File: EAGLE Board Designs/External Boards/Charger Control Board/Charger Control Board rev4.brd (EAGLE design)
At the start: 81 parts

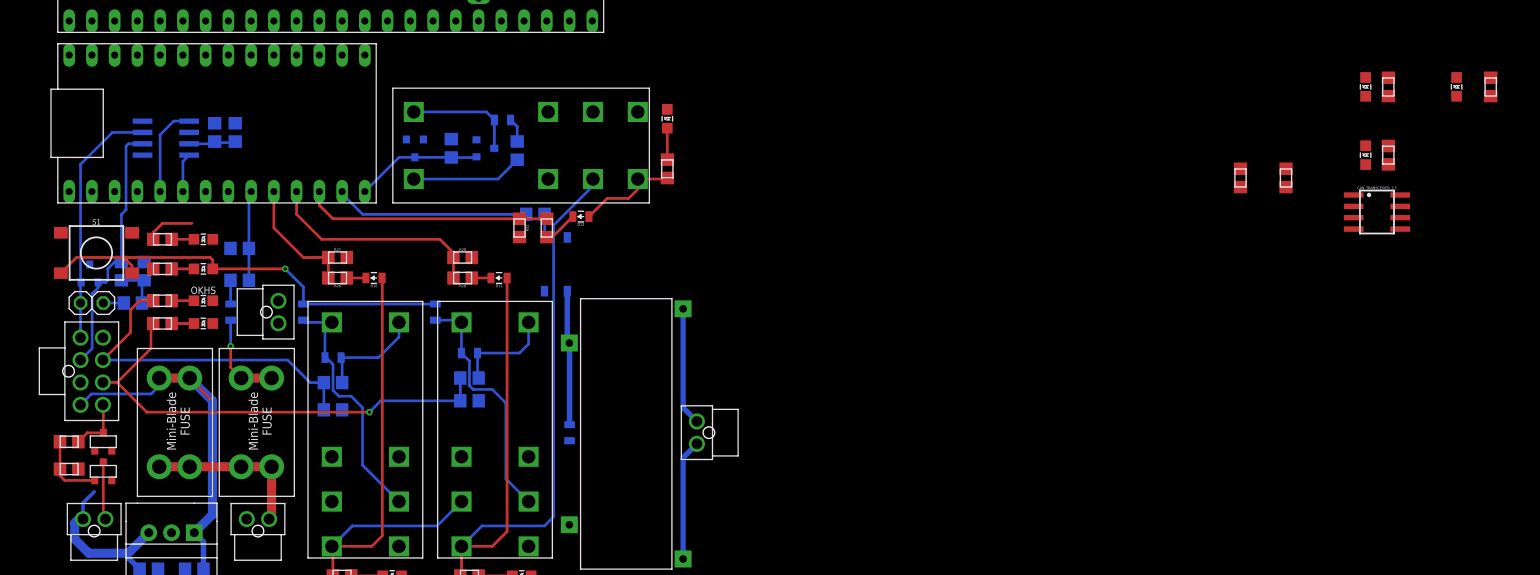
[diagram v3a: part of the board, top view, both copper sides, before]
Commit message: routed all LEDs
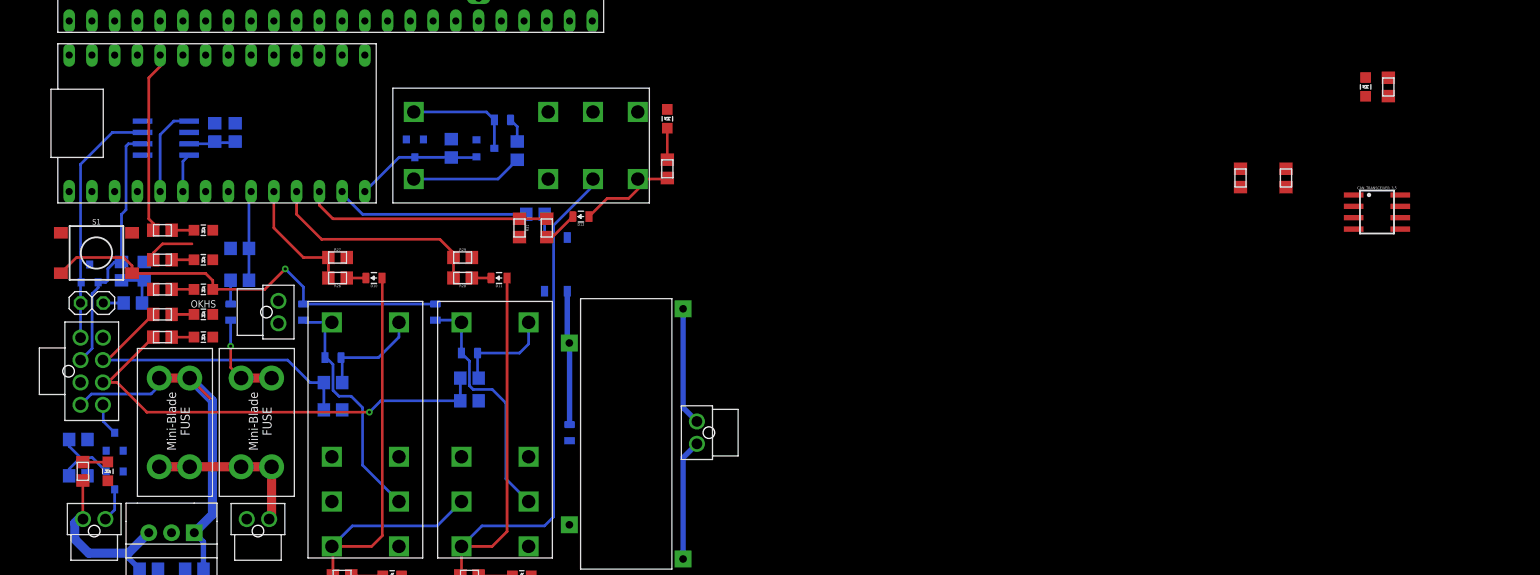
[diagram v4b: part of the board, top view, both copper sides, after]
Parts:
- moved R5 163.0 mm to (-74.7, 34.5), turned to 90 degrees
- moved POWER_5V 156.6 mm to (-71.9, 34.5), turned to 180 degrees
- moved R15 137.2 mm to (-65.8, 61.5), turned to 180 degrees
- moved STATUS_3.2 130.1 mm to (-61.2, 61.5), turned to 270 degrees
- moved LATCH 2.29 mm to (-61.2, 54.9)
- moved R34 2.29 mm to (-65.8, 58.2)
- moved R6 2.29 mm to (-65.8, 54.9)
- moved SOFTWARE 2.29 mm to (-61.2, 58.2)
- moved Q1 1.63 mm to (-71.1, 33.5), flipped to the bottom, turned to 180 degrees
- moved BMS_OK 1.52 mm to (-61.2, 49.5)
- moved OKHS 1.52 mm to (-61.2, 52.1)
- moved R7 1.52 mm to (-65.8, 52.1)
- moved R8 1.52 mm to (-65.8, 49.5)
- moved R12 1.27 mm to (-75.2, 34.0), flipped to the bottom, turned to 0 degrees
- moved ZENER 1.27 mm to (-71.1, 37.8), flipped to the bottom
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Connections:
- net N$11: now also U$4.A8; no longer U$4.A6
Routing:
- net N$11: track 0.00 -> 20.3 mm
- net N$29: track 0.00 -> 2.80 mm
- net N$1: track 6.43 -> 3.75 mm
- net CHARGE_ENABLE: track 6.34 -> 3.67 mm, vias 0 -> 1
- net N$8: track 0.00 -> 2.50 mm
- net OKHS: track 38.6 -> 36.8 mm
- net BMS_OK: track 52.9 -> 51.8 mm
- net +5V: track 23.9 -> 24.7 mm
- net N$5: track 7.91 -> 8.62 mm

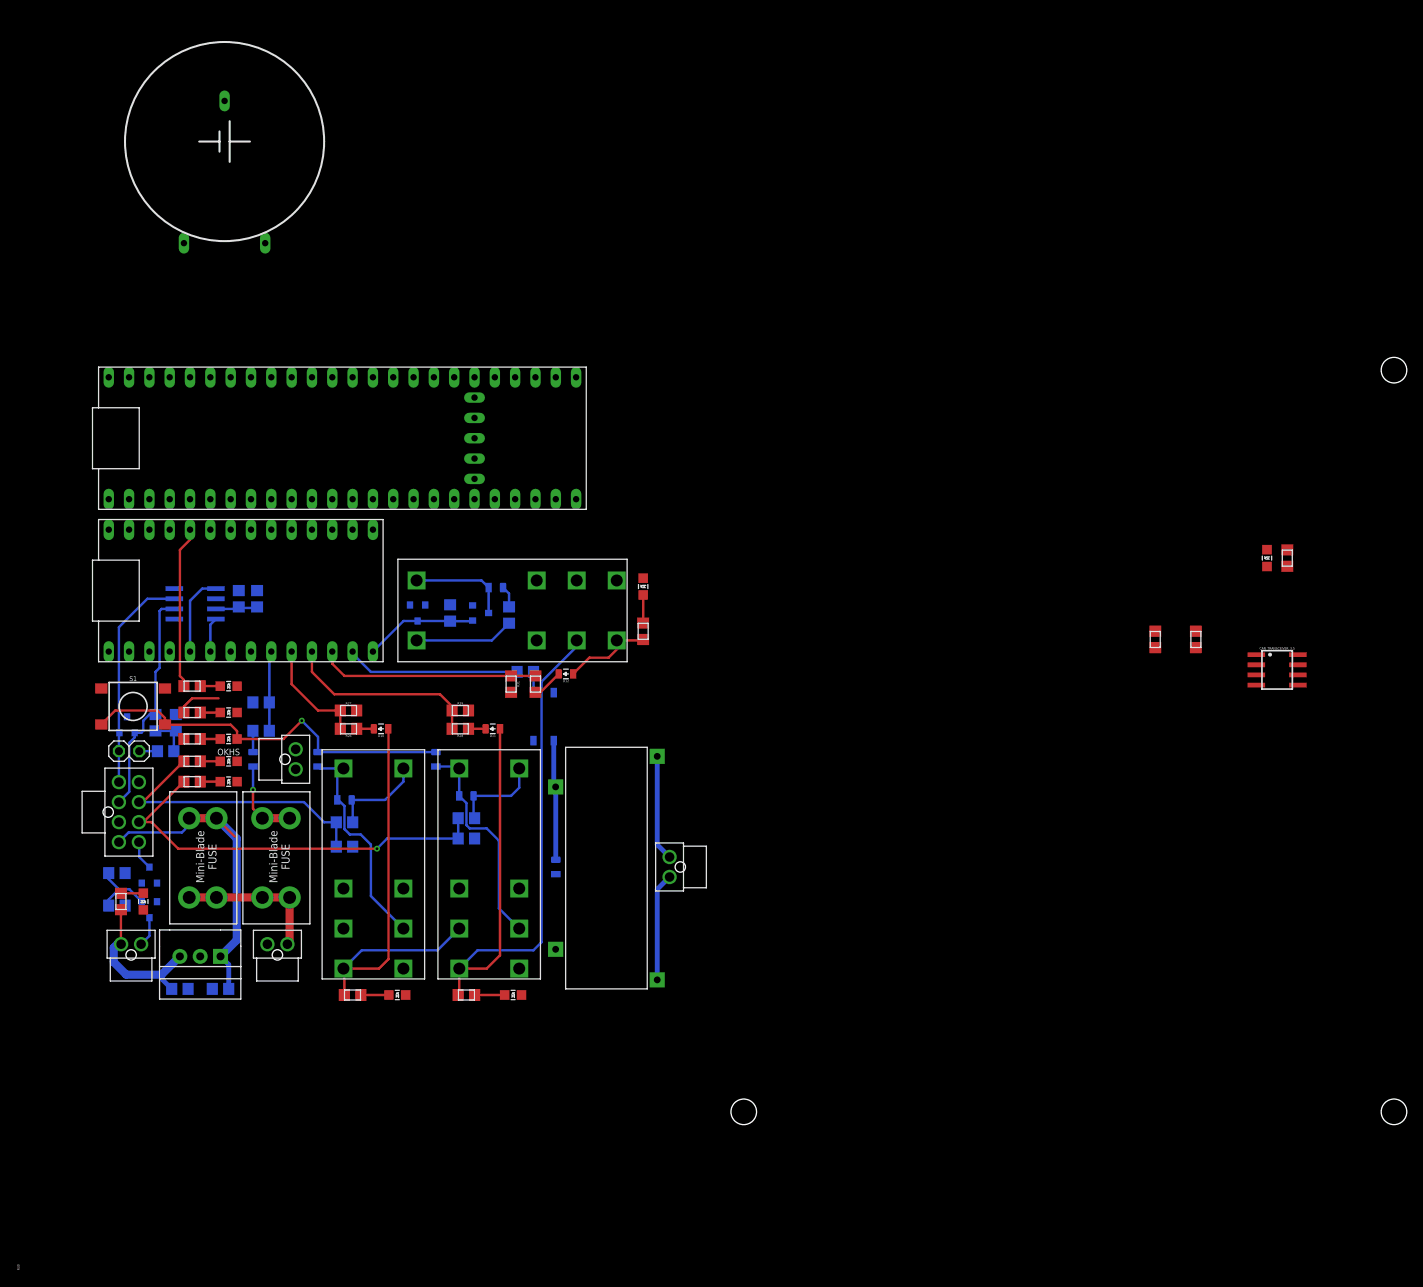
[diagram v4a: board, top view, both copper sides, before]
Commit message: Added ground plane
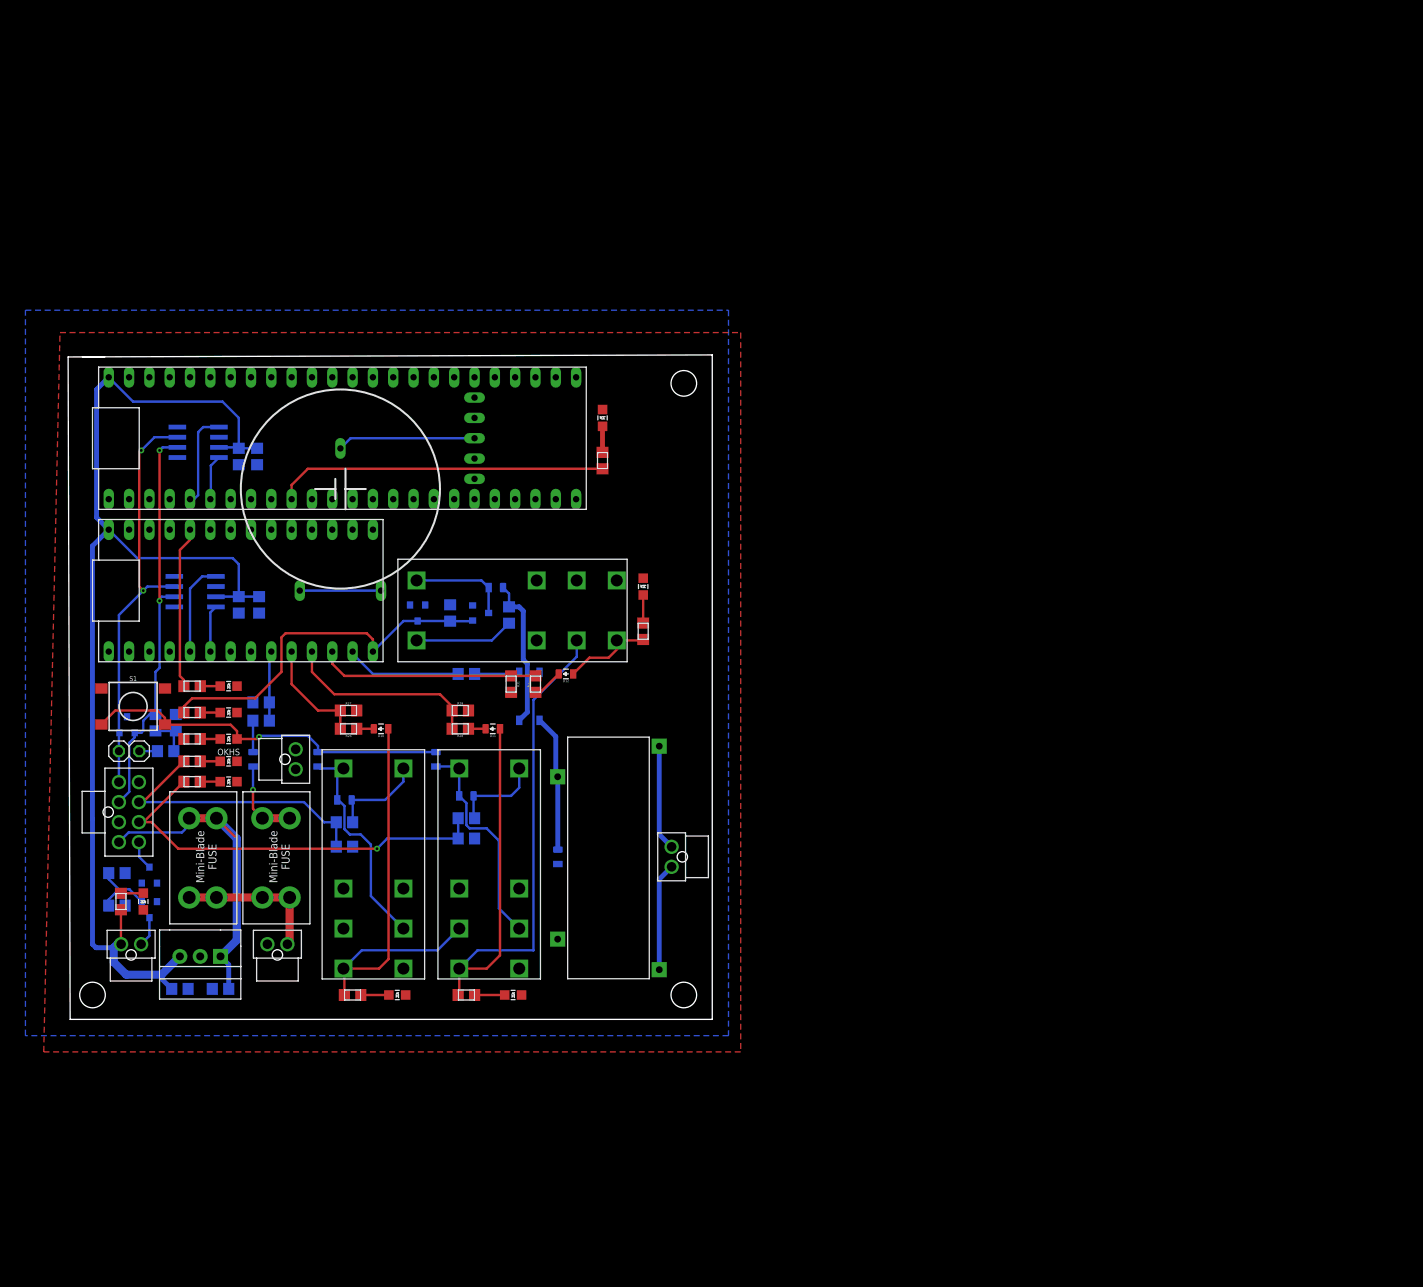
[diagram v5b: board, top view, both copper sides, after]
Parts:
- moved CAN_TRANSCEIVER_3.5 137.8 mm to (-65.0, 91.9), flipped to the bottom
- moved C6 121.8 mm to (-59.9, 90.2), flipped to the bottom, turned to 90 degrees
- moved C7 114.6 mm to (-57.7, 90.2), flipped to the bottom, turned to 90 degrees
- moved R17 86.5 mm to (-14.5, 89.7), turned to 270 degrees
- moved STATUS_3.5 84.9 mm to (-14.5, 95.0)
- moved U$16 45.8 mm to (-47.2, 86.1)
- moved R14 7.37 mm to (-31.5, 63.0)
- moved U$2 3.10 mm to (-23.6, 60.2)
- moved CAN_TRANSCEIVER_3.2 1.52 mm to (-65.4, 73.3)
- moved U$3 1.30 mm to (-8.64, 24.9)
- moved CHARGER 1.30 mm to (-5.84, 40.1)
- moved D3 1.30 mm to (-20.1, 40.1)
- moved R19 1.27 mm to (-57.1, 57.1)
- moved C1 0.80 mm to (-57.4, 71.6), turned to 90 degrees
- moved C2 0.76 mm to (-59.9, 71.6), turned to 90 degrees
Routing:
- net +5V: track 24.7 -> 149.5 mm
- net N$9: track 0.00 -> 41.5 mm
- net SOFTWARE_SHUTDOWN: track 19.6 -> 46.6 mm
- net CANH: track 27.9 -> 52.4 mm, vias 0 -> 2
- net CANL: track 28.9 -> 51.6 mm, vias 0 -> 2
- net N$61: track 0.00 -> 17.3 mm
- net +12V: track 43.5 -> 59.8 mm
- net N$6: track 0.00 -> 12.0 mm
- net VBAT_RTC: track 0.00 -> 10.2 mm
- net TOGGLE_CHARGER: track 21.8 -> 14.5 mm
- net N$4: track 0.00 -> 5.65 mm
- net N$7: track 0.00 -> 3.26 mm
- net N$10: track 2.59 -> 5.66 mm
- net LATCH_EXT_BUTTON: track 48.8 -> 46.5 mm
- net CHARGE_CONTROL: track 15.1 -> 17.2 mm
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- added copper zone on layer 1, net GND
- added copper zone on layer 16, net GND
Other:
- board outline added: 80.5 x 83.1 mm

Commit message: Pass DRC
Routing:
- net +12V: track 59.8 -> 107.2 mm, vias 0 -> 1
- net SHUTDOWN_D: track 11.3 -> 54.9 mm, vias 0 -> 2
- net SHUTDOWN_E: track 0.00 -> 25.1 mm
- net VBAT_RTC: track 10.2 -> 30.9 mm
- net SHUTDOWN_A: track 10.4 -> 27.9 mm
- net GND: track 0.00 -> 16.0 mm, vias 0 -> 1
- net +5V: track 149.5 -> 161.5 mm, vias 0 -> 1
- net CHARGE_ENABLE: track 3.67 -> 7.01 mm, vias 1 -> 0

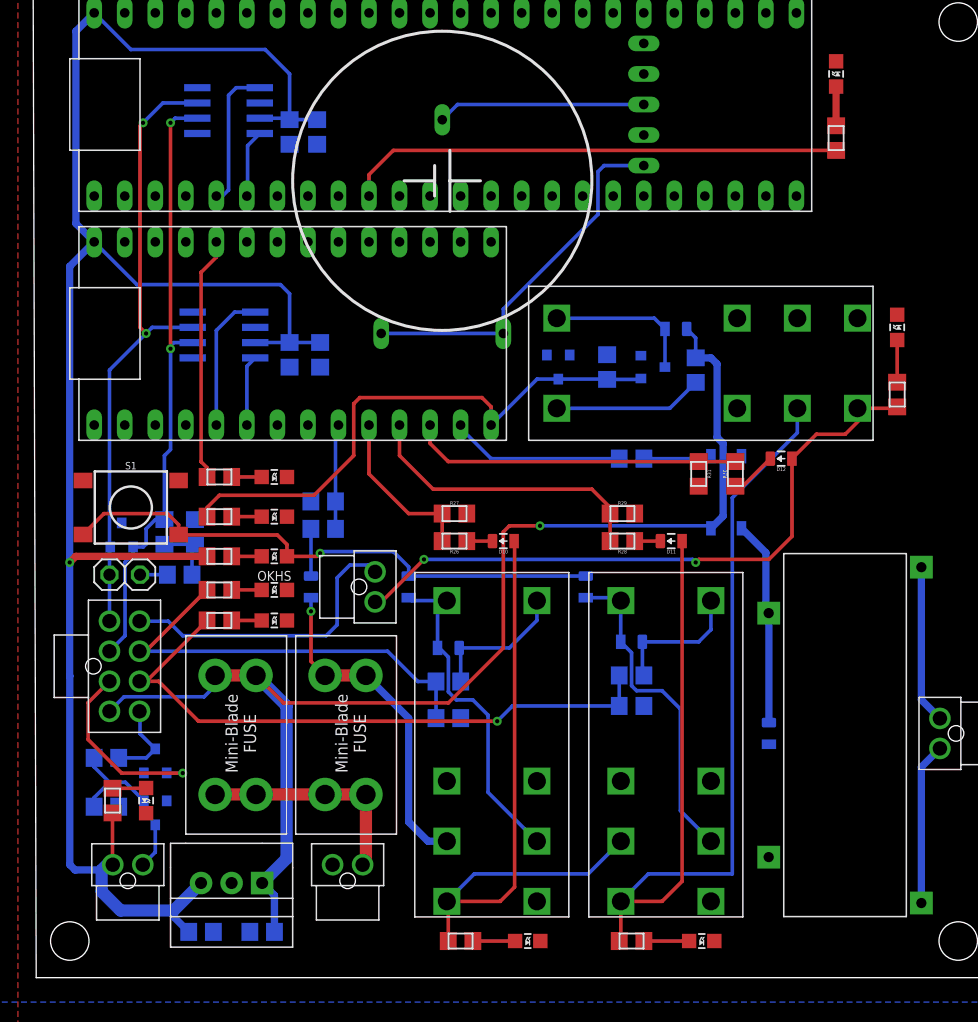
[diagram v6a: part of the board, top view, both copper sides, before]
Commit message: Made 0805 0603
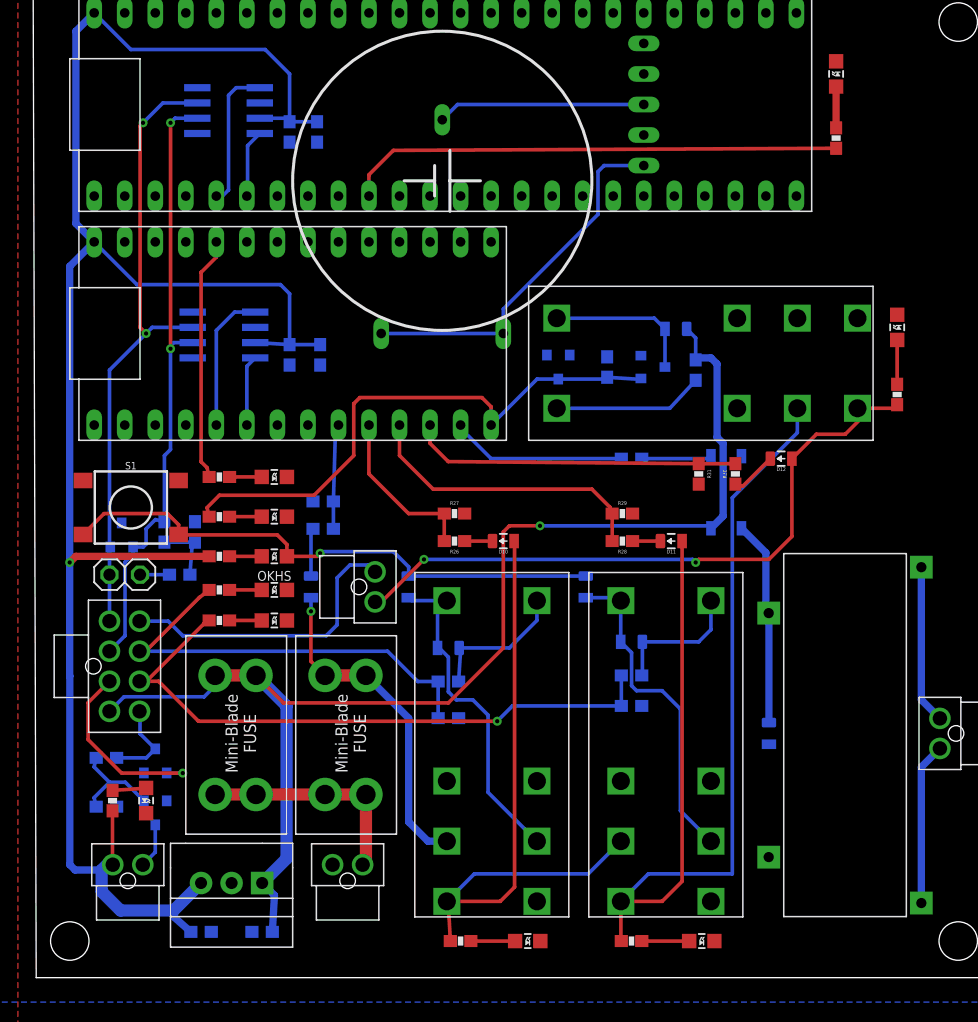
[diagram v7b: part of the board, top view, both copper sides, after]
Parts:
- C1, C2, C3, C4, C5, C6, C7: device HyTechDevices:0805 -> HyTechDevices:0603-CAP
- R1, R10, R11, R12, R13, R14, R15, R16, R17, R18, R19, R2, R20, R26, R27, R28, R29, R3, R30, R31, R34, R35, R36, R4, R5, R6, R7, R8, R9: device HyTechDevices:0805 -> HyTechDevices:0603-RES
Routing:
- net +5V: track 161.5 -> 162.5 mm
